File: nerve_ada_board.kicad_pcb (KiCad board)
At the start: 4 copper layers, 100 x 100 mm, 64 parts, among them J1 TC2050-IDC, J10 PC1-3, J11 PB4-5, J12 Camera, J2 472192001, J3 2171750001, J6 WS2812B, J7 CAN1, J8 CAN2, J9 PA4-7, SW1 SPST, SW2 SPST, SW3 SPST, U1 ld39150dt33-r, U10 TXB0104QPWRQ1, U2 STM32F446RET, U4 SAM-M10Q, U5 XBP9B-DMWT-002, U9 TXB0104QPWRQ1, Y1 8M, Y2 32k768

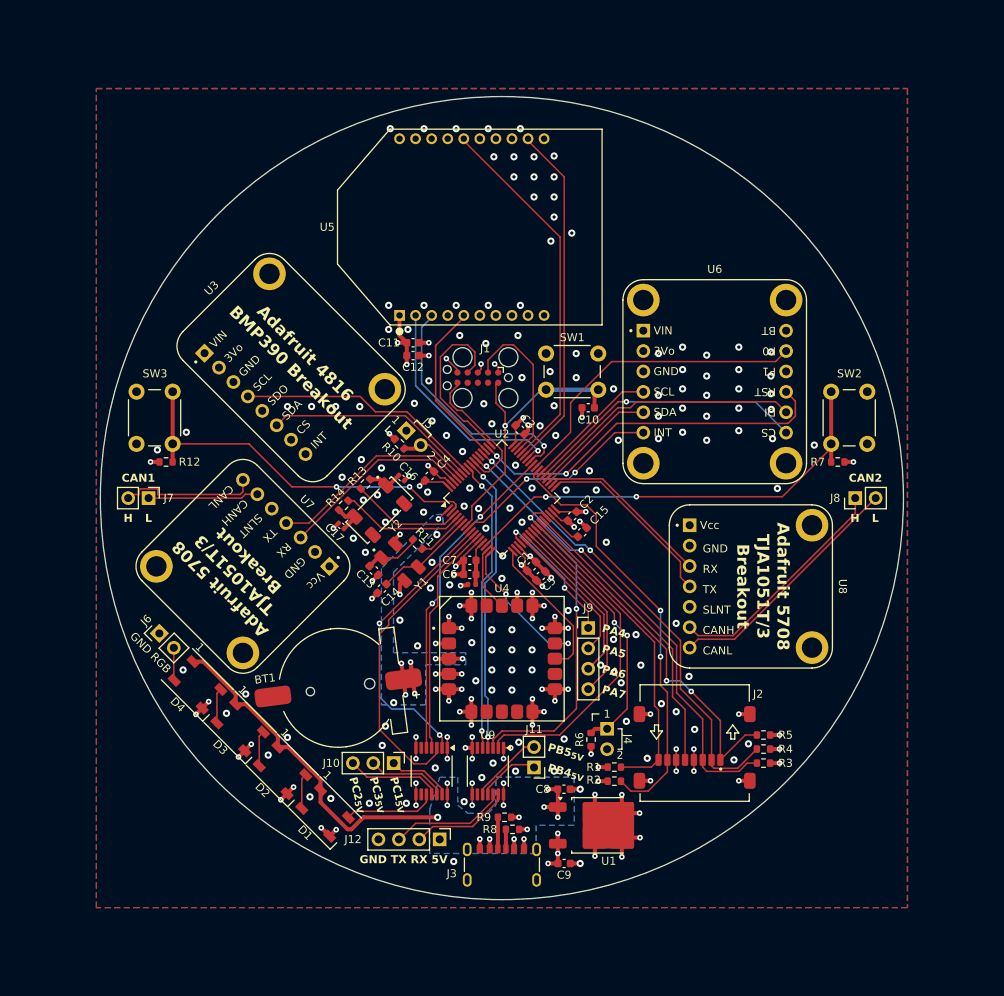
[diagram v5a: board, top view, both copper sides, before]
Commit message: Move LEDs to 4 corners, cleanup layout
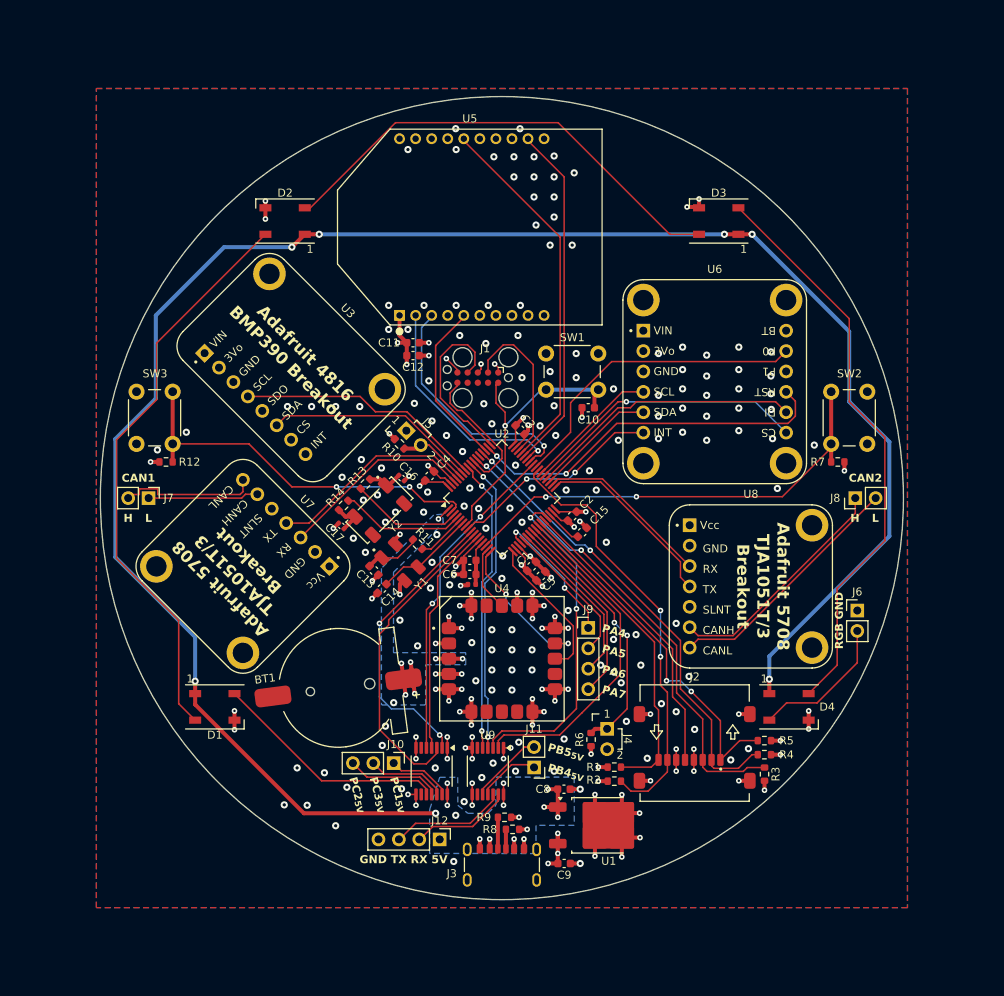
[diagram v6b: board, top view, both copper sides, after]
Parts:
- moved J6 86.9 mm to (192.8, 119.0), turned to 0 degrees
- moved D3 86.8 mm to (175.5, 70.5), turned to 180 degrees
- moved D4 73.7 mm to (184.2, 131.0), turned to 0 degrees
- moved D2 68.4 mm to (121.5, 70.5), turned to 180 degrees
- moved D1 19.0 mm to (112.8, 131.0), turned to 0 degrees
- moved R3 1.38 mm to (181.2, 139.4), turned to 90 degrees
- moved R4 0.71 mm to (181.2, 136.9)
- moved R5 0.71 mm to (181.2, 135.2)
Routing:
- net +5V: track 57.3 -> 253.5 mm, vias 10 -> 16
- net Net-(D1-DOUT): track 4.38 -> 72.2 mm
- net Net-(D3-DOUT): track 4.38 -> 72.0 mm
- net Net-(D2-DOUT): track 4.43 -> 59.2 mm
- net /RGB_LED: track 11.5 -> 29.5 mm
- net Net-(D4-DOUT): track 4.07 -> 17.9 mm
- net /SDIO_CMD: track 58.4 -> 59.1 mm
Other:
- board text added: "RGB GND"
- board text removed: "GND RGB"

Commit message: Add mounting holes and cleanup layout
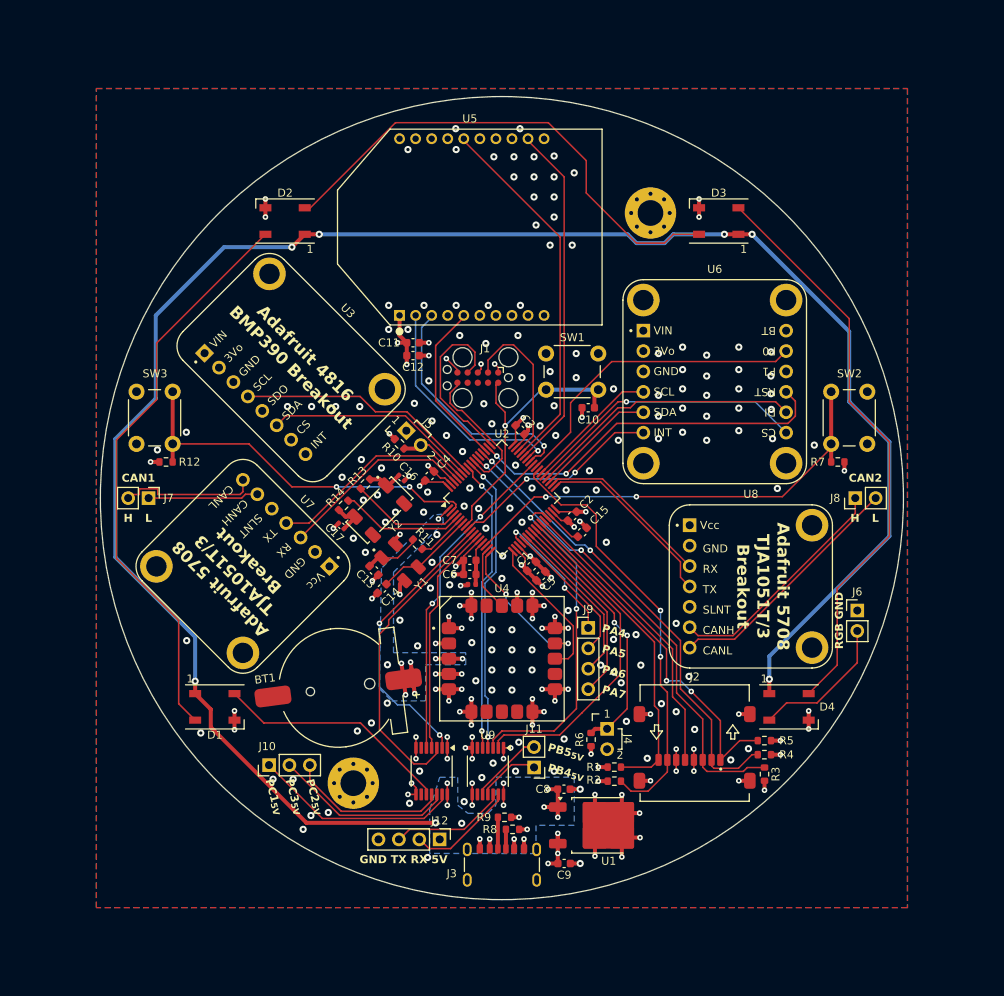
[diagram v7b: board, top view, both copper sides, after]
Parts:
- added H1: M3, MountingHole:MountingHole_3.2mm_M3_Pad_Via, F.Cu at (130.0, 140.5)
- added H2: M3, MountingHole:MountingHole_3.2mm_M3_Pad_Via, F.Cu at (167.0, 69.5)
- moved J10 15.5 mm to (119.5, 138.2), turned to 90 degrees
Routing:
- net /PC1_EXP: track 8.18 -> 26.0 mm
- net /PC2_EXP: track 9.93 -> 22.5 mm
- net /PC3_EXP: track 11.8 -> 19.9 mm
- net Net-(D2-DOUT): track 59.2 -> 62.5 mm
- net +5V: track 253.5 -> 255.4 mm
- net /CAMERA_RX: track 12.5 -> 13.5 mm
- net /PC1: track 36.5 -> 35.7 mm
- net GND: track 126.9 -> 126.7 mm, vias 231 -> 233
